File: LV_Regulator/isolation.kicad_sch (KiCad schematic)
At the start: 21 parts, among them IC1 UCC12040DVE, J1 430450400, J2 430450800, J3 430450400, J4 430450800, K1 41.52.9.005.0010, Q1 BC807, U1 ADM2483xRW

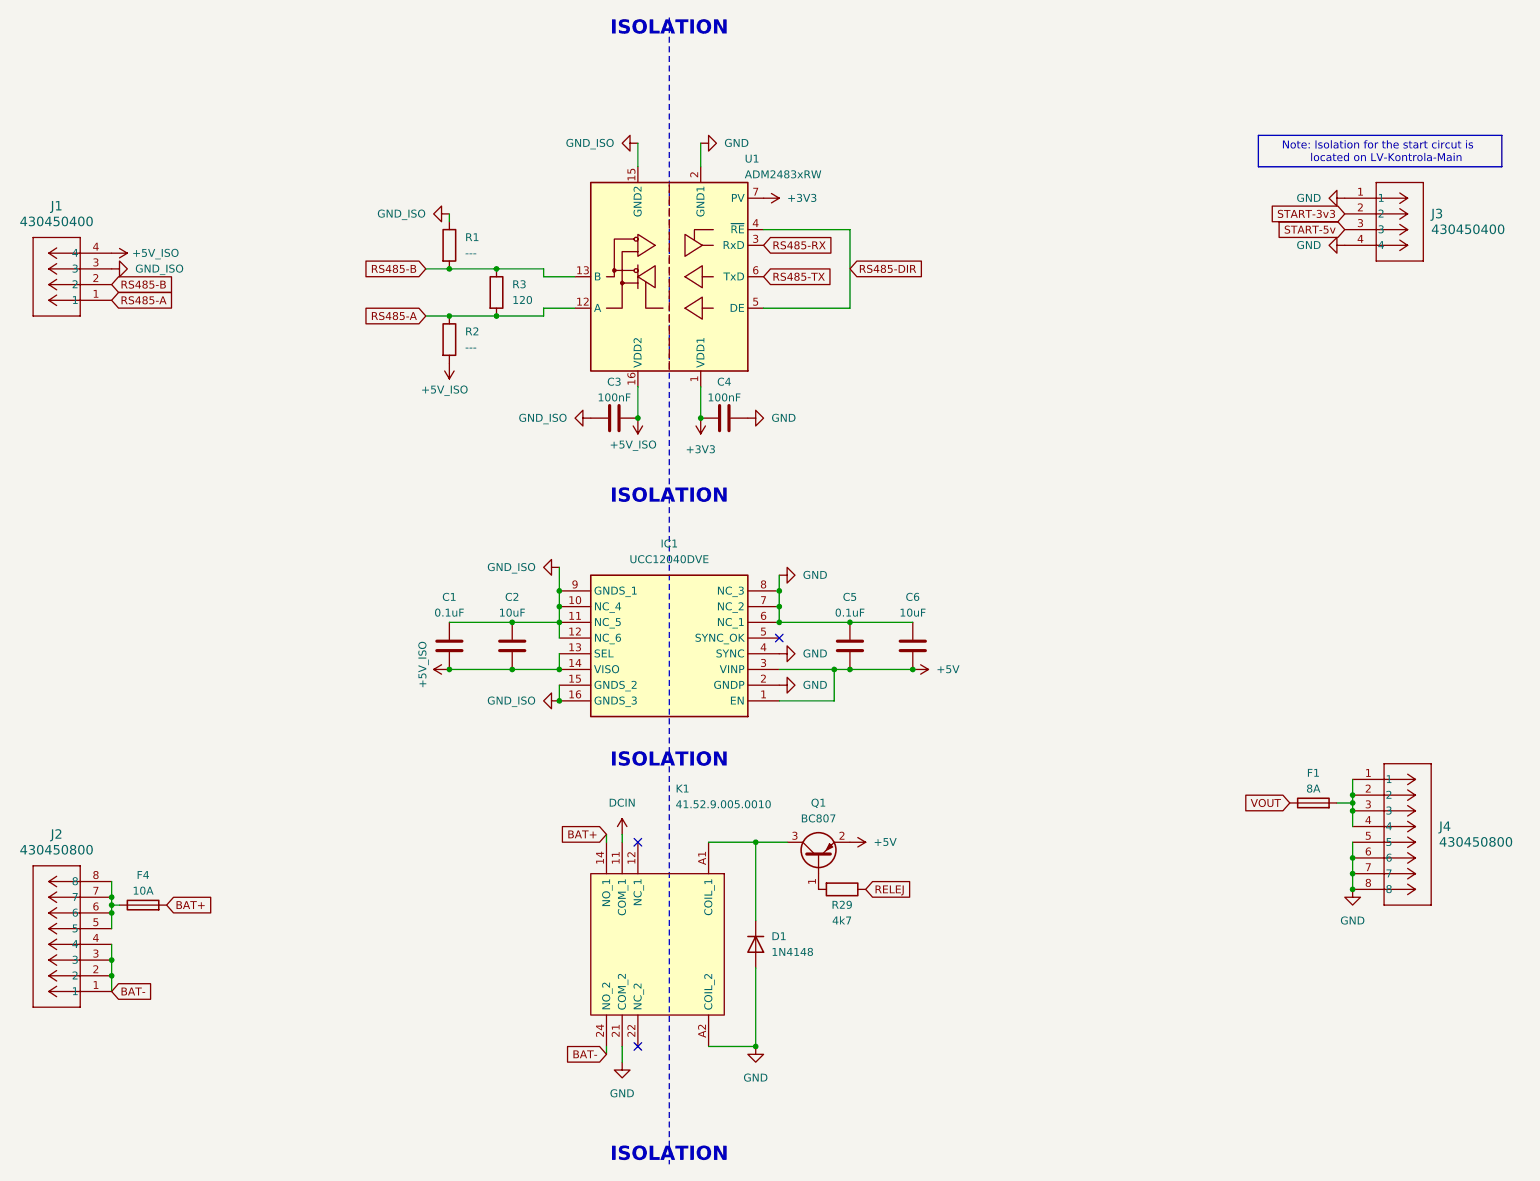
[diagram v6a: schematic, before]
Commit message: Halfway Push of adding 3D models to PCB layout components
Pushing with components left to add to finish on main PC
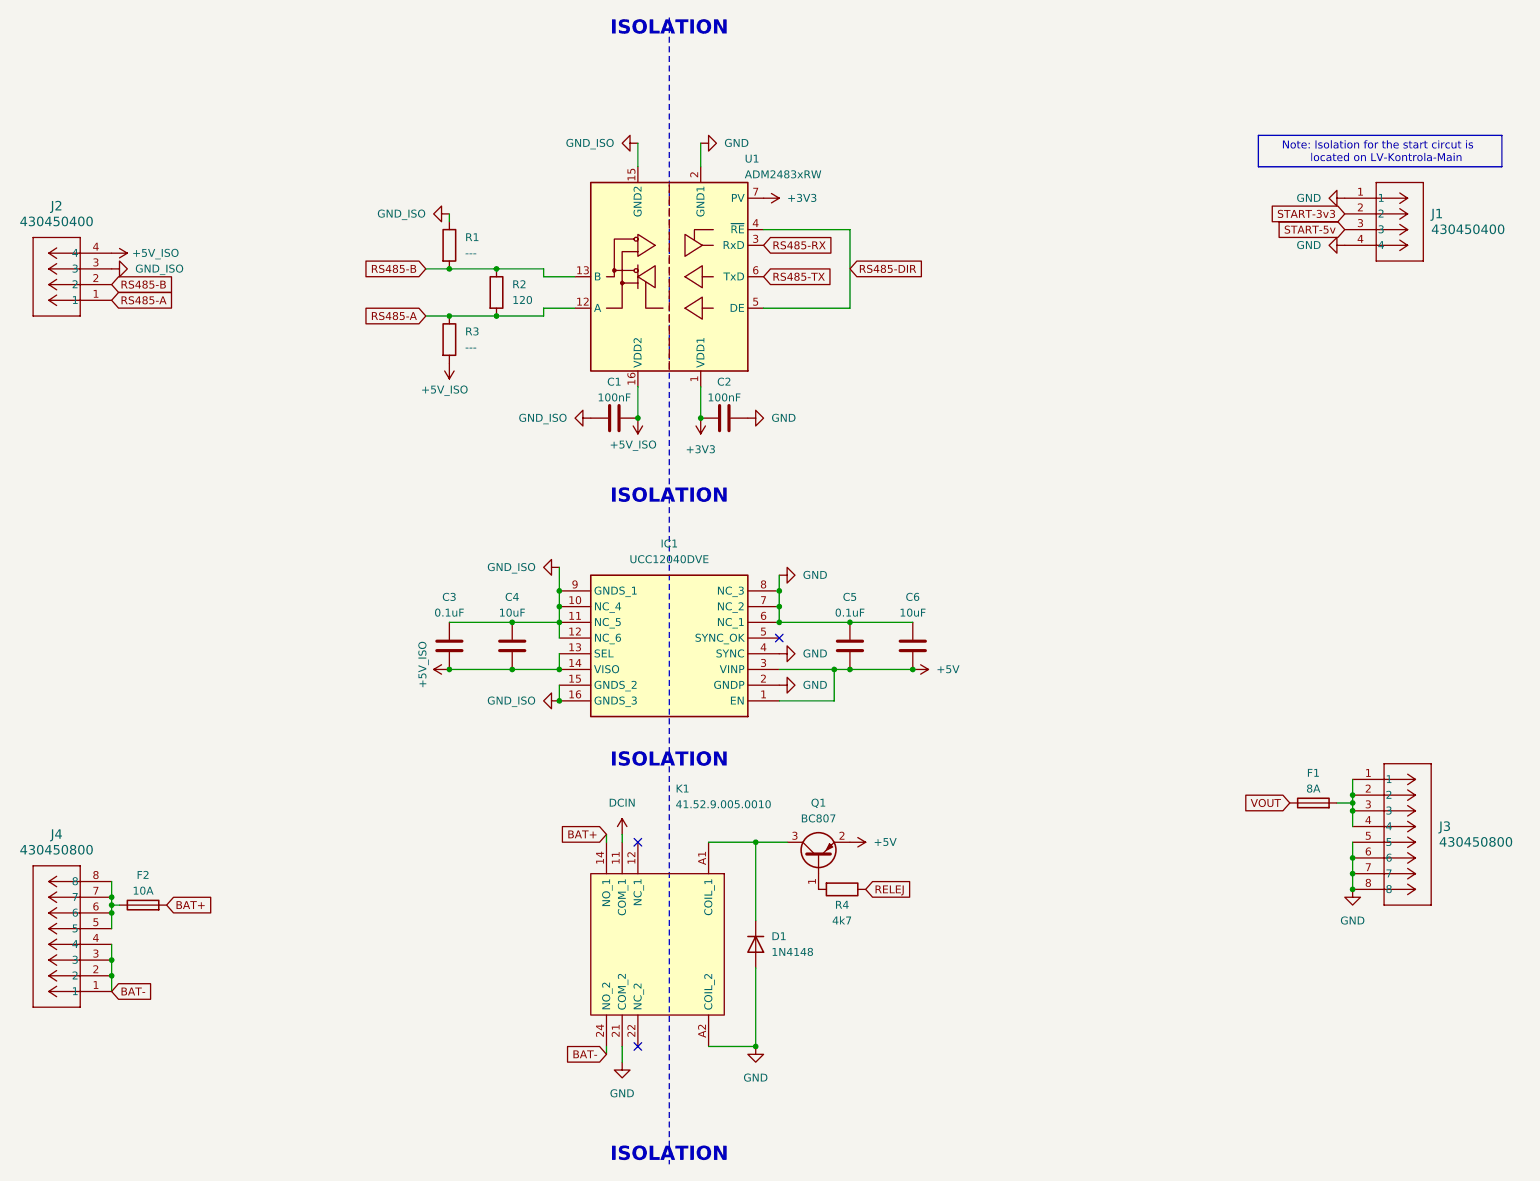
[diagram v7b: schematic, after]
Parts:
- renumbered C3 to C1, C4 to C2, C1 to C3, C2 to C4, F4 to F2, J3 to J1, J1 to J2, J4 to J3, J2 to J4, R3 to R2, R2 to R3, R29 to R4

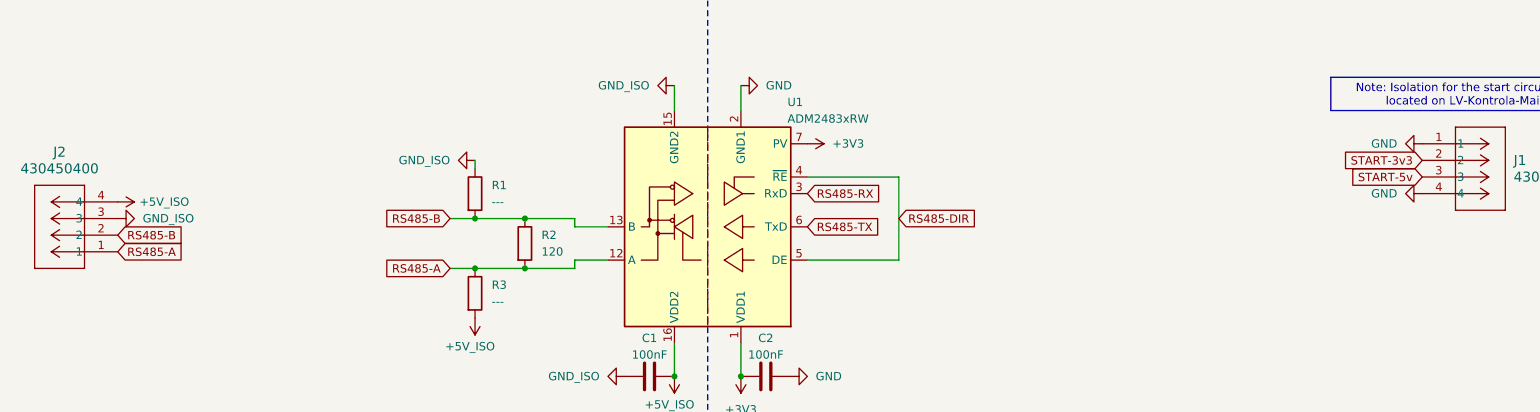
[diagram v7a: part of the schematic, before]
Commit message: Initial Routing for tje LV_Regulator control portion
Changes to the schematic were made for simpler routing
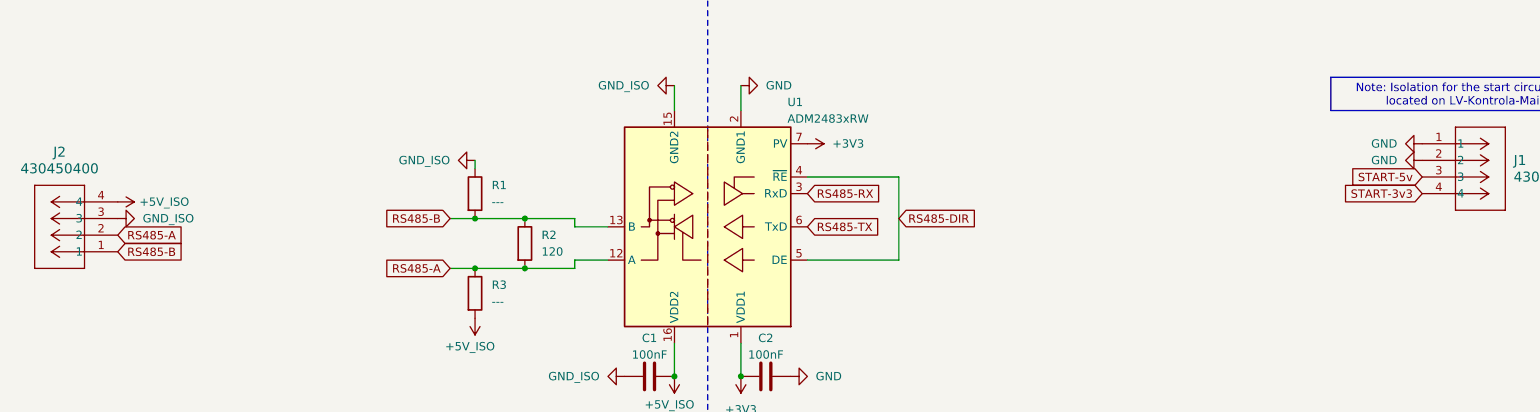
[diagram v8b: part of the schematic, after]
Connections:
- net GND: now also J1.2; no longer J1.4
- net RS485-A: now also J2.2; no longer J2.1
- net RS485-B: now also J2.1; no longer J2.2
- net START-3v3: now also J1.4; no longer J1.2
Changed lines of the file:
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@@
+		)
+	)
+	(global_label "RS485-B"
+		(shape input)
+		(at 45.72 58.42 0)
+		(fields_autoplaced yes)
+		(effects
+			(font
+				(size 1.27 1.27)
+			)
+			(justify left)
+		)
+		(property "Intersheetrefs" "${INTERSHEET_REFS}"
+			(at 57.6556 58.42 0)
+			(effects
+				(font
+					(size 1.27 1.27)
+				)
+				(justify left)
+				(hide yes)
+			)
+		)
+	)
+	(global_label "RS485-A"
+		(shape input)
+		(at 45.72 55.88 0)
+		(fields_autoplaced yes)
+		(effects
+			(font
+				(size 1.27 1.27)
+			)
+			(justify left)
+		)
+		(property "Intersheetrefs" "${INTERSHEET_REFS}"
+			(at 57.4742 55.88 0)
+			(effects
+				(font
+					(size 1.27 1.27)
+				)
+				(justify left)
+				(hide yes)
+			)
 		)
 	)
@@
 		)
 	)
-	(global_label "RS485-A"
+	(global_label "BAT-"
 		(shape input)
-		(at 45.72 58.42 0)
+		(at 45.72 170.18 0)
 		(fields_autoplaced yes)
 		(effects
@@
 		)
 		(property "Intersheetrefs" "${INTERSHEET_REFS}"
-			(at 57.4742 58.42 0)
-			(effects
-				(font
-					(size 1.27 1.27)
-				)
-				(justify left)
-				(hide yes)
-			)
-		)
-	)
-	(global_label "BAT-"
+			(at 53.6038 170.18 0)
+			(effects
+				(font
+					(size 1.27 1.27)
+				)
+				(justify left)
+				(hide yes)
+			)
+		)
+	)
+	(global_label "START-3v3"
 		(shape input)
-		(at 45.72 170.18 0)
+		(at 245.11 49.53 180)
 		(fields_autoplaced yes)
 		(effects
@@
 				(size 1.27 1.27)
 			)
-			(justify left)
+			(justify right)
 		)
 		(property "Intersheetrefs" "${INTERSHEET_REFS}"
-			(at 53.6038 170.18 0)
-			(effects
-				(font
-					(size 1.27 1.27)
-				)
-				(justify left)
-				(hide yes)
-			)
-		)
-	)
-	(global_label "RS485-B"
+			(at 231.6625 49.53 0)
+			(effects
+				(font
+					(size 1.27 1.27)
+				)
+				(justify right)
+				(hide yes)
+			)
+		)
+	)
+	(global_label "VOUT"
 		(shape input)
-		(at 45.72 55.88 0)
+		(at 236.22 139.7 180)
 		(fields_autoplaced yes)
 		(effects
@@
 				(size 1.27 1.27)
 			)
-			(justify left)
+			(justify right)
 		)
 		(property "Intersheetrefs" "${INTERSHEET_REFS}"
-			(at 57.6556 55.88 0)
-			(effects
-				(font
-					(size 1.27 1.27)
-				)
-				(justify left)
-				(hide yes)
-			)
-		)
-	)
-	(global_label "START-3v3"
+			(at 228.5176 139.7 0)
+			(effects
+				(font
+					(size 1.27 1.27)
+				)
+				(justify right)
+				(hide yes)
+			)
+		)
+	)
+	(global_label "RELEJ"
 		(shape input)
-		(at 245.11 44.45 180)
+		(at 167.64 153.67 0)
 		(fields_autoplaced yes)
 		(effects
@@
 				(size 1.27 1.27)
 			)
-			(justify right)
-		)
-		(property "Intersheetrefs" "${INTERSHEET_REFS}"
-			(at 231.6625 44.45 0)
-			(effects
-				(font
-					(size 1.27 1.27)
-				)
-				(justify right)
-				(hide yes)
-			)
-		)
-	)
-	(global_label "VOUT"
-		(shape input)
-		(at 236.22 139.7 180)
-		(fields_autoplaced yes)
-		(effects
-			(font
-				(size 1.27 1.27)
-			)
-			(justify right)
-		)
-		(property "Intersheetrefs" "${INTERSHEET_REFS}"
-			(at 228.5176 139.7 0)
-			(effects
-				(font
-					(size 1.27 1.27)
-				)
-				(justify right)
-				(hide yes)
-			)
-		)
-	)
-	(global_label "RELEJ"
-		(shape input)
-		(at 167.64 153.67 0)
-		(fields_autoplaced yes)
-		(effects
-			(font
-				(size 1.27 1.27)
-			)
 			(justify left)
 		)
@@
 	(symbol
 		(lib_id "power:GND")
-		(at 245.11 49.53 270)
+		(at 245.11 44.45 270)
 		(unit 1)
 		(exclude_from_sim no)
@@
 		(fields_autoplaced yes)
 		(property "Reference" "#PWR06"
-			(at 238.76 49.53 0)
+			(at 238.76 44.45 0)
 			(effects
 				(font
@@
 		)
 		(property "Value" "GND"
-			(at 241.3 49.5299 90)
+			(at 241.3 44.4499 90)
 			(effects
 				(font
@@
 		)
 		(property "Footprint" ""
-			(at 245.11 49.53 0)
+			(at 245.11 44.45 0)
 			(effects
 				(font
@@
 		)
 		(property "Datasheet" ""
-			(at 245.11 49.53 0)
+			(at 245.11 44.45 0)
 			(effects
 				(font
@@
 		)
 		(property "Description" "Power symbol creates a global label with name \"GND\" , ground"
-			(at 245.11 49.53 0)
-			(effects
-				(font
-					(size 1.27 1.27)
-				)
-				(hide yes)
-			)
-		)
-		(pin "1"
-		)
-		(instances
-			(project ""
+			(at 245.11 44.45 0)
+			(effects
+				(font
+					(size 1.27 1.27)
+				)
+				(hide yes)
+			)
+		)
+		(pin "1"
+		)
+		(instances
+			(project "LV_Regulator"
 				(path "/9003ce10-3354-47c9-924a-fd038a206791/91e40ea1-1eda-495a-bc23-83cea8129846"
 					(reference "#PWR06")
